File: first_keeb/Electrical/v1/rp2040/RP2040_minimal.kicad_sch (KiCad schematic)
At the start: 72 parts, among them J1 Conn_01x04_Socket, P1 USB-TYPE-C-016, Q1 BSS138, SW1 TS-1187A-B-A-B, SW2 TS-1187A-B-A-B, SW3 BUTT1, SW4 BUTT3, SW5 BUTT2, U1 PRTR5V0U2X, U2 ME6208A44M3G, U3 RP2040, U4 ME6212C25M5G, U5 W25Q16JVSS, U6 ME6212C33M5G, U7 SLSS49E, U8 SLSS49E, U9 SLSS49E, Y1 12MHz

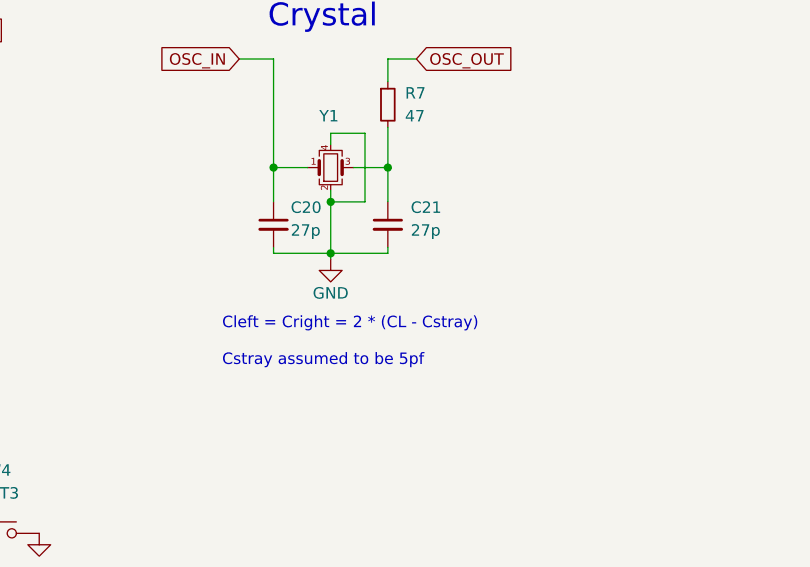
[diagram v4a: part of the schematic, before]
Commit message: changes caps to match 12MHz crystal
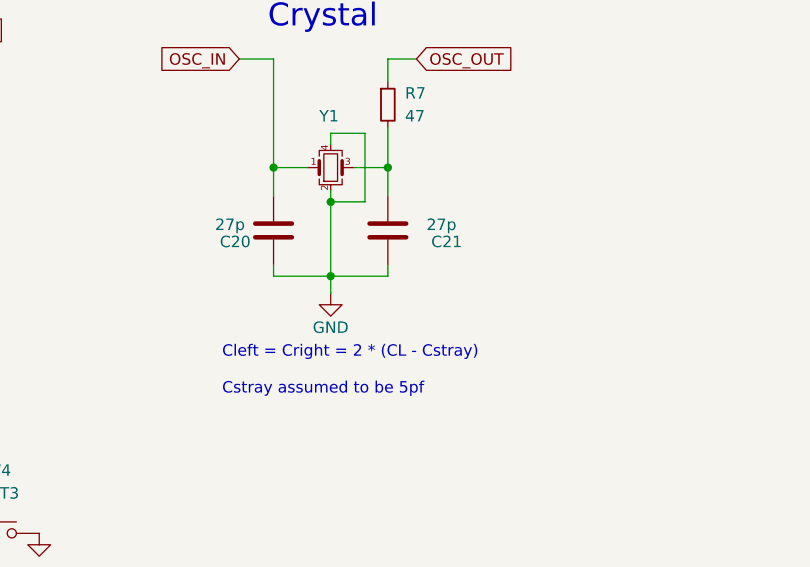
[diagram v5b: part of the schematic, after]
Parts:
- removed C20, C21: 27p, Capacitor_SMD:C_0402_1005Metric, symbol Device:C_Small
- added C20, C21: 27p, Capacitor_SMD:C_0402_1005Metric, symbol Device:C
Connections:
- net GND: now also C20.1, C21.1
- net OSC_IN: now also C20.2
- net at R7.2, Y1.3: now also C21.2
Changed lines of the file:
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@@
   (junction (at 281.305 140.97) (diameter 0) (color 0 0 0 0)
   )
-  (junction (at 194.945 182.88) (diameter 0) (color 0 0 0 0)
+  (junction (at 194.945 185.42) (diameter 0) (color 0 0 0 0)
   )
   (junction (at 183.515 255.905) (diameter 0) (color 0 0 0 0)
@@
     (stroke (width 0) (type default))
   )
-  (wire (pts (xy 201.295 182.88) (xy 201.295 182.245))
-    (stroke (width 0) (type default))
-  )
   (wire (pts (xy 350.52 115.57) (xy 352.425 115.57))
     (stroke (width 0) (type default))
@@
     (stroke (width 0) (type default))
   )
-  (wire (pts (xy 194.945 177.165) (xy 194.945 182.88))
+  (wire (pts (xy 194.945 177.165) (xy 194.945 185.42))
     (stroke (width 0) (type default))
   )
@@
     (stroke (width 0) (type default))
   )
-  (wire (pts (xy 188.595 182.88) (xy 188.595 182.245))
+  (wire (pts (xy 188.595 185.42) (xy 188.595 184.15))
     (stroke (width 0) (type default))
   )
@@
     (stroke (width 0) (type default))
   )
-  (wire (pts (xy 194.945 183.515) (xy 194.945 182.88))
+  (wire (pts (xy 194.945 187.325) (xy 194.945 185.42))
     (stroke (width 0) (type default))
   )
@@
     (stroke (width 0) (type default))
   )
-  (wire (pts (xy 194.945 182.88) (xy 201.295 182.88))
+  (wire (pts (xy 194.945 185.42) (xy 201.295 185.42))
     (stroke (width 0) (type default))
   )
@@
     (stroke (width 0) (type default))
   )
-  (wire (pts (xy 194.945 182.88) (xy 188.595 182.88))
+  (wire (pts (xy 194.945 185.42) (xy 188.595 185.42))
     (stroke (width 0) (type default))
   )
@@
     (stroke (width 0) (type default))
   )
-  (wire (pts (xy 188.595 177.165) (xy 188.595 173.355))
+  (wire (pts (xy 188.595 176.53) (xy 188.595 173.355))
     (stroke (width 0) (type default))
   )
@@
     (stroke (width 0) (type default))
   )
+  (wire (pts (xy 201.295 184.15) (xy 201.295 185.42))
+    (stroke (width 0) (type default))
+  )
   (wire (pts (xy 125.095 254) (xy 125.095 255.905))
     (stroke (width 0) (type default))
@@
     (stroke (width 0) (type default))
   )
-  (wire (pts (xy 201.295 177.165) (xy 201.295 173.355))
+  (wire (pts (xy 201.295 173.355) (xy 201.295 176.53))
     (stroke (width 0) (type default))
   )
@@
   )
   (text "Cleft = Cright = 2 * (CL - Cstray)\n\nCstray assumed to be 5pf"
-    (at 182.88 195.58 0)
+    (at 182.88 198.755 0)
     (effects (font (size 1.27 1.27)) (justify left bottom))
   )
@@
     )
   )
-  (symbol (lib_id "Device:C_Small") (at 188.595 179.705 0) (unit 1)
-    (in_bom yes) (on_board yes) (dnp no)
-    (property "Reference" "C20" (at 190.5 177.8 0)
-      (effects (font (size 1.27 1.27)) (justify left))
-    )
-    (property "Value" "27p" (at 190.5 180.34 0)
-      (effects (font (size 1.27 1.27)) (justify left))
-    )
-    (property "Footprint" "Capacitor_SMD:C_0402_1005Metric" (at 188.595 179.705 0)
-      (effects (font (size 1.27 1.27)) hide)
-    )
-    (property "Datasheet" "~" (at 188.595 179.705 0)
-      (effects (font (size 1.27 1.27)) hide)
-    )
-    (property "LCSC Part #" "" (at 188.595 179.705 0)
-      (effects (font (size 1.27 1.27)) hide)
-    )
-    (pin "1")
-    (pin "2")
-    (instances
-      (project "RP2040_minimal"
-        (path "/26e500cb-9f3f-4e62-bb26-21a6be4a5bcc"
-          (reference "C20") (unit 1)
-        )
-      )
-      (project "STM32F4_REV2"
-        (path "/6ea106a1-bff5-4b72-bf63-92640b003eed"
-          (reference "C15") (unit 1)
-        )
-      )
-    )
-  )
   (symbol (lib_id "power:VBUS") (at 328.295 55.245 0) (unit 1)
     (in_bom yes) (on_board yes) (dnp no)
@@
     )
   )
-  (symbol (lib_id "power:GND") (at 194.945 183.515 0) (unit 1)
+  (symbol (lib_id "power:GND") (at 194.945 187.325 0) (unit 1)
     (in_bom yes) (on_board yes) (dnp no)
-    (property "Reference" "#PWR037" (at 194.945 189.865 0)
+    (property "Reference" "#PWR037" (at 194.945 193.675 0)
       (effects (font (size 1.27 1.27)) hide)
     )
-    (property "Value" "GND" (at 194.945 187.325 0)
+    (property "Value" "GND" (at 194.945 191.135 0)
       (effects (font (size 1.27 1.27)))
     )
-    (property "Footprint" "" (at 194.945 183.515 0)
+    (property "Footprint" "" (at 194.945 187.325 0)
       (effects (font (size 1.27 1.27)) hide)
     )
-    (property "Datasheet" "" (at 194.945 183.515 0)
+    (property "Datasheet" "" (at 194.945 187.325 0)
       (effects (font (size 1.27 1.27)) hide)
     )
@@
     )
   )
+  (symbol (lib_id "Device:C") (at 201.295 180.34 180) (unit 1)
+    (in_bom yes) (on_board yes) (dnp no)
+    (property "Reference" "C21" (at 209.55 181.61 0)
+      (effects (font (size 1.27 1.27)) (justify left))
+    )
+    (property "Value" "27p" (at 208.915 179.705 0)
+      (effects (font (size 1.27 1.27)) (justify left))
+    )
+    (property "Footprint" "Capacitor_SMD:C_0402_1005Metric" (at 200.3298 176.53 0)
+      (effects (font (size 1.27 1.27)) hide)
+    )
+    (property "Datasheet" "~" (at 201.295 180.34 0)
+      (effects (font (size 1.27 1.27)) hide)
+    )
+    (pin "1")
+    (pin "2")
+    (instances
+      (project "RP2040_minimal"
+        (path "/26e500cb-9f3f-4e62-bb26-21a6be4a5bcc"
+          (reference "C21") (unit 1)
+        )
+      )
+    )
+  )
   (symbol (lib_id "power:GND") (at 166.37 128.27 0) (unit 1)
     (in_bom yes) (on_board yes) (dnp no)
@@
     )
   )
+  (symbol (lib_id "Device:C") (at 188.595 180.34 180) (unit 1)
+    (in_bom yes) (on_board yes) (dnp no)
+    (property "Reference" "C20" (at 186.055 181.61 0)
+      (effects (font (size 1.27 1.27)) (justify left))
+    )
+    (property "Value" "27p" (at 185.42 179.705 0)
+      (effects (font (size 1.27 1.27)) (justify left))
+    )
+    (property "Footprint" "Capacitor_SMD:C_0402_1005Metric" (at 187.6298 176.53 0)
+      (effects (font (size 1.27 1.27)) hide)
+    )
+    (property "Datasheet" "~" (at 188.595 180.34 0)
+      (effects (font (size 1.27 1.27)) hide)
+    )
+    (pin "1")
+    (pin "2")
+    (instances
+      (project "RP2040_minimal"
+        (path "/26e500cb-9f3f-4e62-bb26-21a6be4a5bcc"
+          (reference "C20") (unit 1)
+        )
+      )
+    )
+  )
   (symbol (lib_id "Device:C") (at 159.385 36.195 0) (unit 1)
     (in_bom yes) (on_board yes) (dnp no)
@@
         )
       )
-    )
-  )
-  (symbol (lib_id "Device:C_Small") (at 201.295 179.705 0) (unit 1)
-    (in_bom yes) (on_board yes) (dnp no)
-    (property "Reference" "C21" (at 203.835 177.8 0)
-      (effects (font (size 1.27 1.27)) (justify left))
-    )
-    (property "Value" "27p" (at 203.835 180.34 0)
-      (effects (font (size 1.27 1.27)) (justify left))
-    )
-    (property "Footprint" "Capacitor_SMD:C_0402_1005Metric" (at 201.295 179.705 0)
-      (effects (font (size 1.27 1.27)) hide)
-    )
-    (property "Datasheet" "~" (at 201.295 179.705 0)
-      (effects (font (size 1.27 1.27)) hide)
-    )
-    (property "LCSC Part #" "" (at 201.295 179.705 0)
-      (effects (font (size 1.27 1.27)) hide)
-    )
-    (pin "1")
-    (pin "2")
-    (instances
-      (project "RP2040_minimal"
-        (path "/26e500cb-9f3f-4e62-bb26-21a6be4a5bcc"
-          (reference "C21") (unit 1)
-        )
-      )
-      (project "STM32F4_REV2"
-        (path "/6ea106a1-bff5-4b72-bf63-92640b003eed"
-          (reference "C16") (unit 1)
-        )
-      )

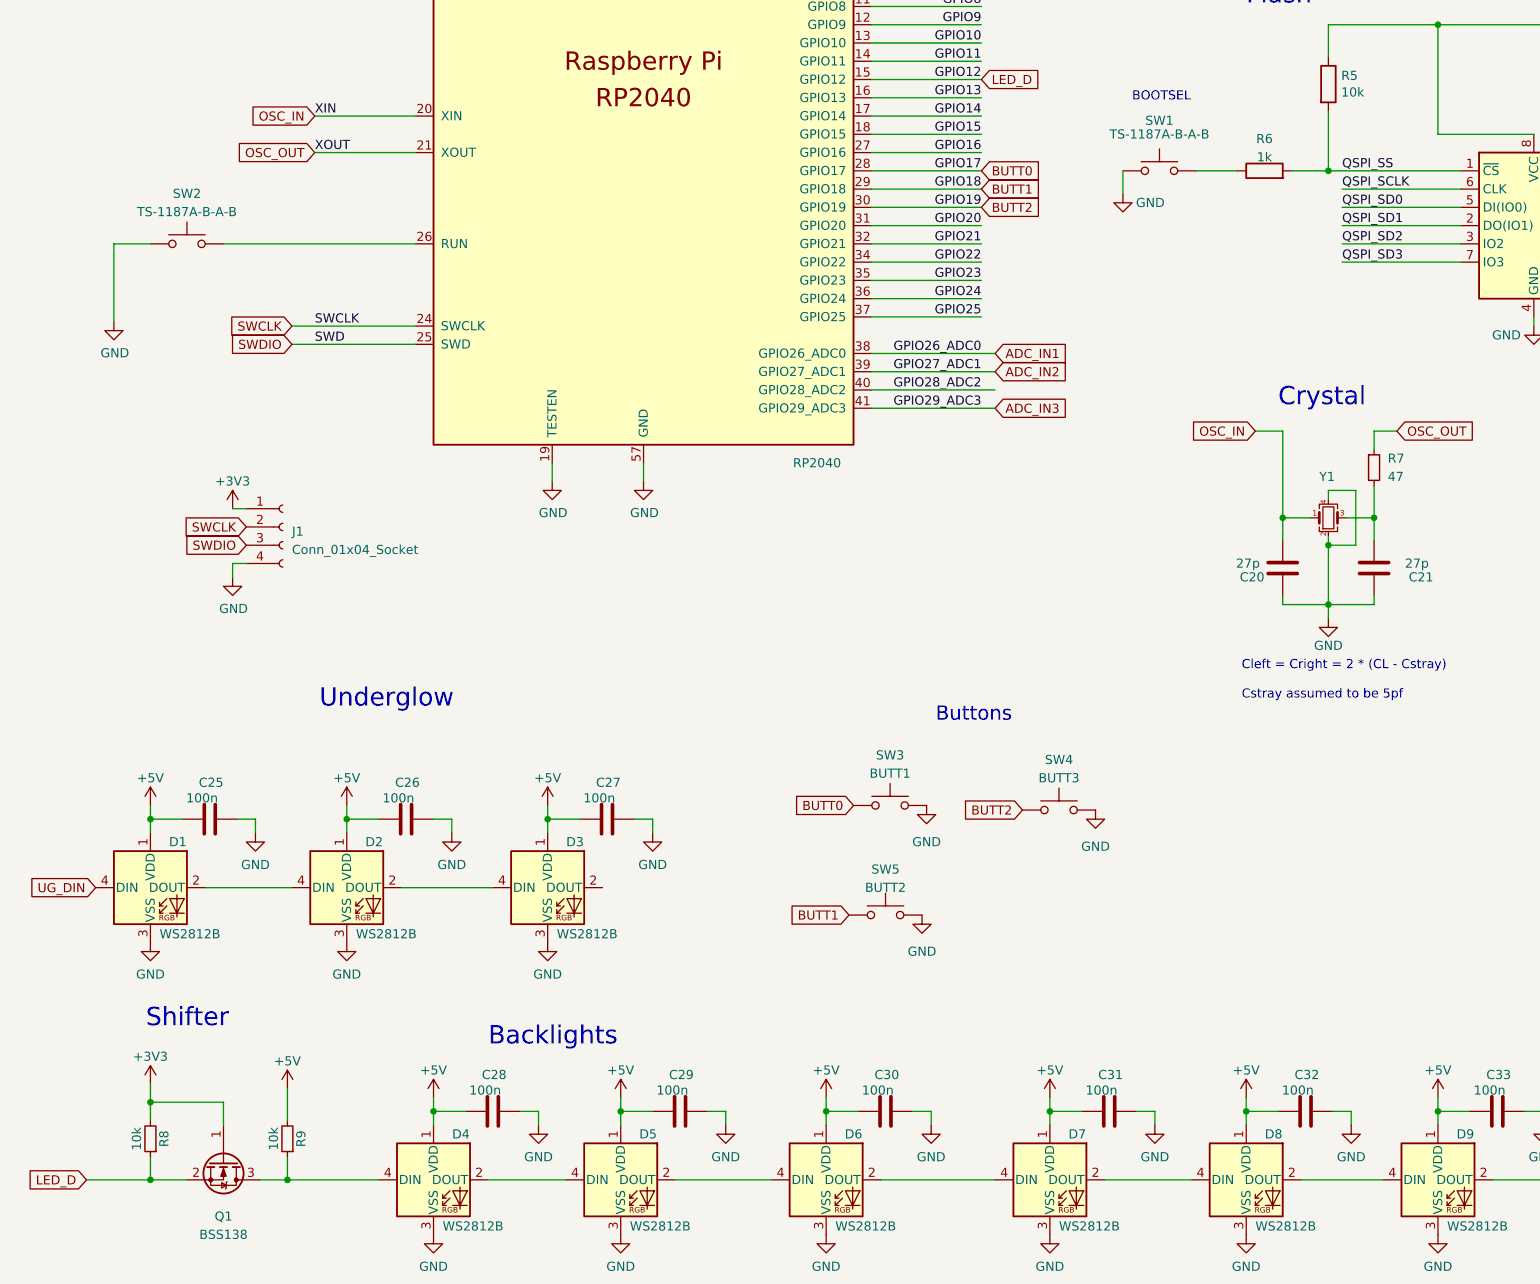
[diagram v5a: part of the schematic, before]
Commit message: adds pullup for run pin
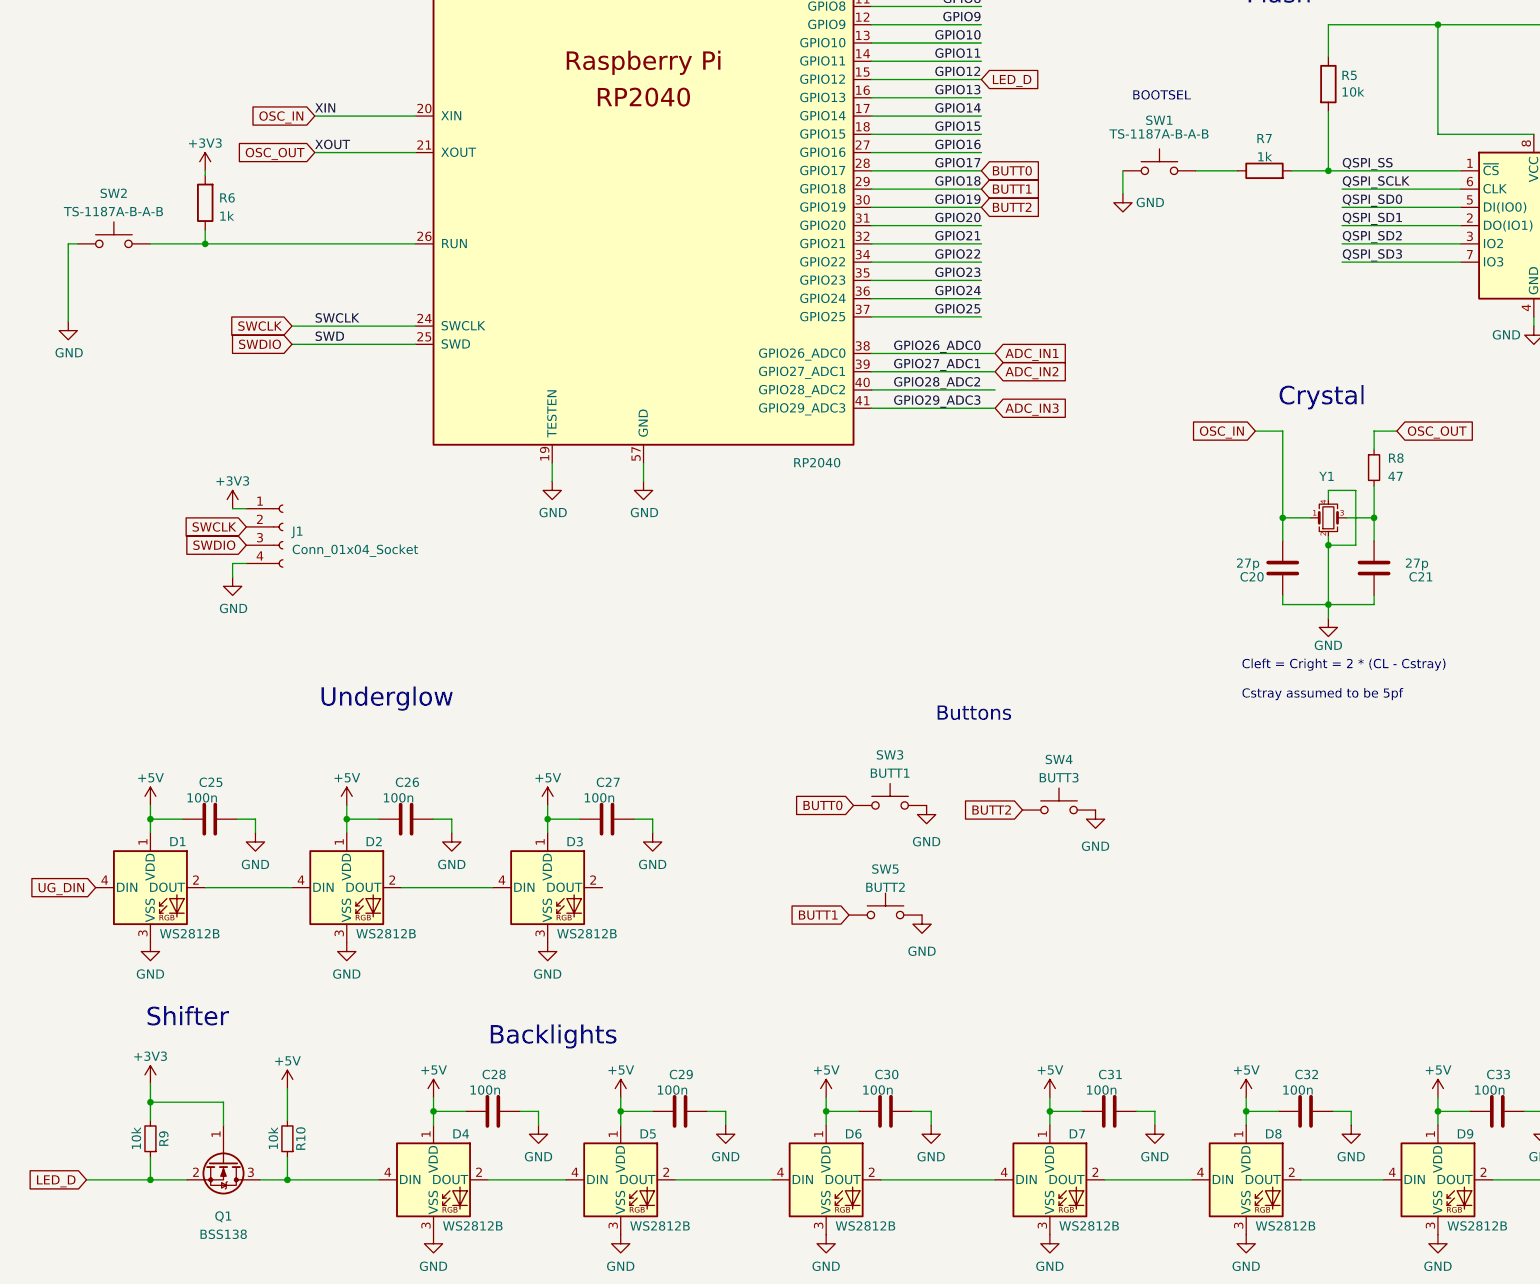
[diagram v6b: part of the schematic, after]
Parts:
- added R6: 1k, Capacitor_SMD:C_0402_1005Metric, symbol Device:R
- renumbered R9 to R10, R6 to R7, R7 to R8, R8 to R9
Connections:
- net +3V3: now also R6.2
- net at SW2.2, U3.26 (RUN): now also R6.1
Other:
- moved on the sheet: SW2
